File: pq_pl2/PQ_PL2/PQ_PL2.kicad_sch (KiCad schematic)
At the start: 70 parts, among them J1 SLW-110-01-T-S, J2 SLW-110-01-T-S, J3 SLW-110-01-T-S, J4 SLW-110-01-T-S, J5 U.FL-R-SMT, J6 MS-156C3, J7 MS-156C3, J8 MS-156C3, J9 MS-156C3, U1 LEE2-6+, U10 TPS613226ADBVT, U11 TPS613226ADBVT, U12 TCN75AVUA713-VAO, U2 LEE2-6+, U3 LM258WDT, U4 ADE-11X+, U5 LEE2-6+, U6 LT5537EDDB, U8 LT1949ES8#PBF, U9 LT1949ES8#PBF

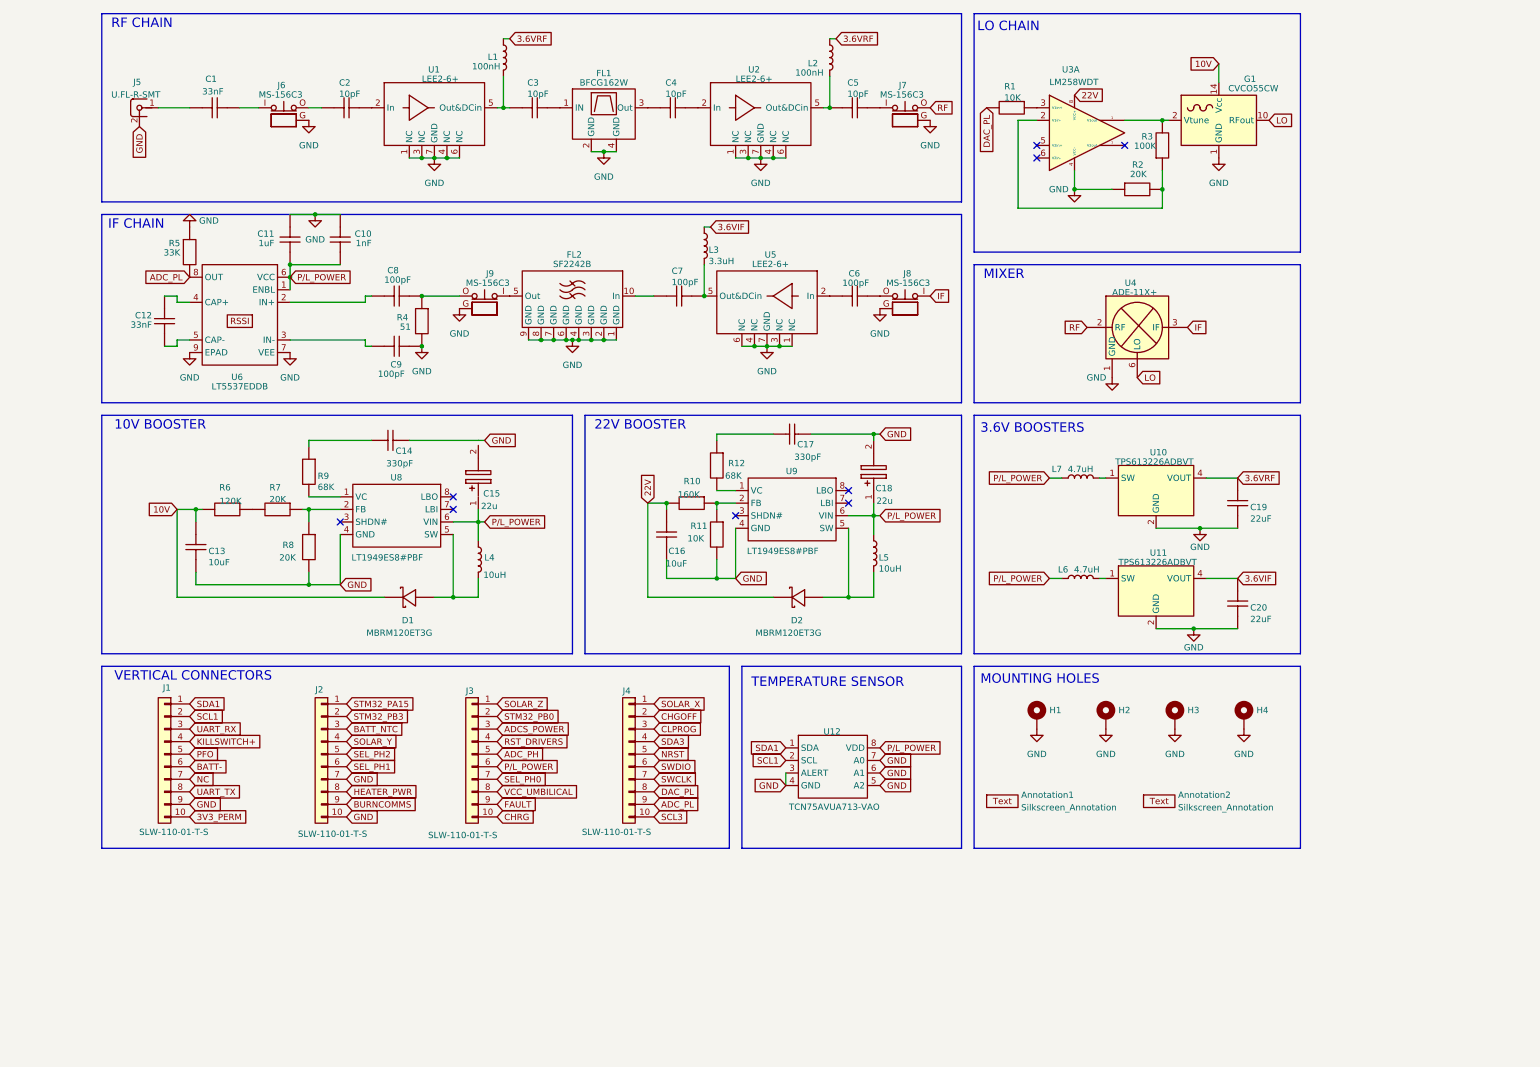
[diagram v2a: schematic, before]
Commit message: P/L2 V03 final schematic. Replaced the Mixer+VCO+Opamp <- OBC DAC configuration with the MAX2121. Switched the IF from 40 MHz (prone to image frequencies due to passive mixers) to 70 MHz with complex mixers with Cheby filter at 75 ohms. Simplified the power supply scheme. Pending PCB & Verification
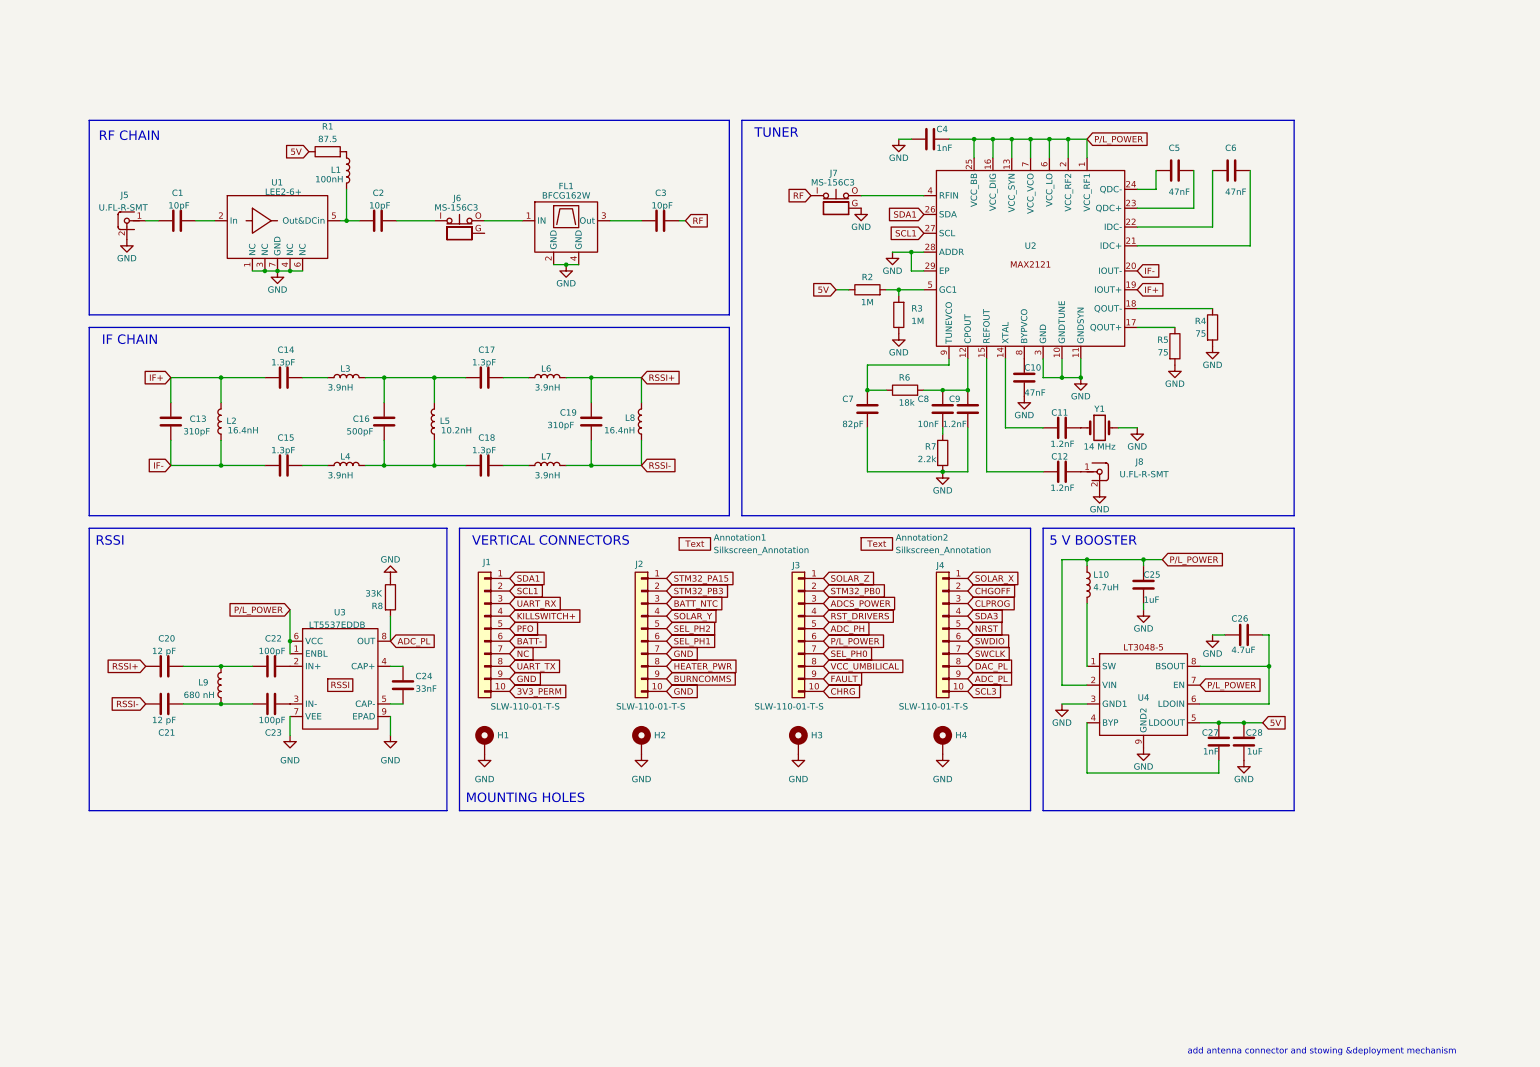
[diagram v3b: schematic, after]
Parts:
- removed C1: 33nF, Capacitor_SMD:C_0603_1608Metric, symbol L2_PCB-altium-import:3_33nF
- removed C10: 1nF, Capacitor_SMD:C_0603_1608Metric, symbol L2_PCB-altium-import:2_1nF
- removed C11: 1uF, Capacitor_SMD:C_0603_1608Metric, symbol L2_PCB-altium-import:2_1uF
- removed C13, C16: 10uF, Capacitor_SMD:C_0603_1608Metric, symbol L2_PCB-altium-import:1_10uF
- removed C14: 330pF, Capacitor_SMD:C_0603_1608Metric, symbol L2_PCB-altium-import:0_330pF
- removed C15, C18: 22u, Capacitor_SMD:C_1206_3216Metric, symbol L2_PCB-altium-import:1_22u
- removed C17: 330pF, Capacitor_SMD:C_0603_1608Metric, symbol L2_PCB-altium-import:2_330pF
- removed C19, C20: 22uF, Capacitor_SMD:C_0603_1608Metric, symbol L2_PCB-altium-import:0_22uF
- removed C5: 10pF, Capacitor_SMD:C_0603_1608Metric, symbol L2_PCB-altium-import:0_10pF
- removed C6, C7: 100pF, Capacitor_SMD:C_0603_1608Metric, symbol L2_PCB-altium-import:0_100pF
- removed D1, D2: MBRM120ET3G, -nsl_passive:MBRM120ET3G, symbol passive-nsl:MBRM120ET3G
- removed FL2: SF2242B, -nsl_rf:SF2242B, symbol rf-nsl:SF2242B
- removed G1: CVCO55CW, RF_Mini-Circuits:Mini-Circuits_CK605_LandPatternPL-012, symbol Oscillator:CVCO55xx
- removed J7, J8, J9: MS-156C3, -nsl_connector:CoaxialSwitch_Hirose_MS-156C3_Horizontal, symbol connector-nsl:MS-156C
- removed R1: 10K, Resistor_SMD:R_0603_1608Metric, symbol L2_PCB-altium-import:2_10K
- removed R10: 160K, Resistor_SMD:R_0603_1608Metric, symbol L2_PCB-altium-import:0_160K
- removed R11: 10K, Resistor_SMD:R_0603_1608Metric, symbol L2_PCB-altium-import:1_10K
- removed R12: 68K, Resistor_SMD:R_0603_1608Metric, symbol L2_PCB-altium-import:3_68K
- removed R2: 20K, Resistor_SMD:R_0603_1608Metric, symbol L2_PCB-altium-import:3_20K
- removed R3: 100K, Resistor_SMD:R_0603_1608Metric, symbol L2_PCB-altium-import:1_100K
- removed R4: 51, Resistor_SMD:R_0603_1608Metric, symbol L2_PCB-altium-import:3_51
- removed R6: 120K, Resistor_SMD:R_0603_1608Metric, symbol L2_PCB-altium-import:0_120K
- removed R7: 20K, Resistor_SMD:R_0603_1608Metric, symbol L2_PCB-altium-import:0_20K
- removed R8: 20K, Resistor_SMD:R_0603_1608Metric, symbol L2_PCB-altium-import:1_20K
- removed R9: 68K, Resistor_SMD:R_0603_1608Metric, symbol L2_PCB-altium-import:1_68K
- removed U10, U11: TPS613226ADBVT, Package_TO_SOT_SMD:SOT-23-5, symbol Regulator_Switching:TPS613226ADBV
- removed U12: TCN75AVUA713-VAO, Package_SO:SOP-8_3.9x4.9mm_P1.27mm, symbol SP_ICs:TCN75AVUA713
- removed U2, U5: LEE2-6+, Package_SON:WSON-6-1EP_2x2mm_P0.65mm_EP1x1.6mm, symbol rf-nsl:LEE2-6+
- removed U3: LM258WDT, Package_SO:SO-8_3.9x4.9mm_P1.27mm, symbol power-nsl:LM258
- removed U4: ADE-11X+, -nsl_rf:SOTFL254P691X284-6N, symbol rf-nsl:ADE-11X
- removed U8, U9: LT1949ES8#PBF, Package_SO:SO-8_3.9x4.9mm_P1.27mm, symbol power-nsl:LT1949
- added C10, C5, C6: 47nF, Capacitor_SMD:C_0603_1608Metric, symbol Device:C
- added C11, C12, C9: 1.2nF, Capacitor_SMD:C_0603_1608Metric, symbol Device:C
- added C13, C19: 310pF, Capacitor_SMD:C_0603_1608Metric, symbol Device:C
- added C14, C15, C17, C18: 1.3pF, Capacitor_SMD:C_0603_1608Metric, symbol Device:C
- added C16: 500pF, Capacitor_SMD:C_0603_1608Metric, symbol Device:C
- added C20, C21: 12 pF, Capacitor_SMD:C_0603_1608Metric, symbol Device:C
- added C25, C28: 1uF, Capacitor_SMD:C_0603_1608Metric, symbol Device:C
- added C26: 4.7uF, Capacitor_SMD:C_0603_1608Metric, symbol Device:C
- added C27, C4: 1nF, Capacitor_SMD:C_0603_1608Metric, symbol Device:C
- added C7: 82pF, Capacitor_SMD:C_0603_1608Metric, symbol Device:C
- added C8: 10nF, Capacitor_SMD:C_0603_1608Metric, symbol Device:C
- added J7: MS-156C3, -nsl_connector:CoaxialSwitch_Hirose_MS-156C3_Horizontal, symbol -nsl_connector:MS-156C
- added J8: U.FL-R-SMT, -nsl_connector:C.FL-R-SMT-1(90), symbol -nsl_connector:connector-coax
- added L10: 4.7uH, Inductor_SMD:L_0603_1608Metric, symbol Device:L
- added L8: 16.4nH, Inductor_SMD:L_0603_1608Metric, symbol Device:L
- added L9: 680 nH, Inductor_SMD:L_0603_1608Metric, symbol Device:L
- added R1: 87.5, Resistor_SMD:R_0612_1632Metric, symbol Device:R
- added R2, R3: 1M, Resistor_SMD:R_0612_1632Metric, symbol Device:R
- added R4, R5: 75, Resistor_SMD:R_0612_1632Metric, symbol Device:R
- added R6: 18k, Resistor_SMD:R_0612_1632Metric, symbol Device:R
- added R7: 2.2k, Resistor_SMD:R_0612_1632Metric, symbol Device:R
- added U2: ~, -nsl_rf:QFN50P500X500X80-29N, symbol -nsl_rf:MAX2121
- added U4: ~, -nsl_power:SON45P200X200X80-9N, symbol -nsl_power:LT3048
- added Y1: 14 MHz, symbol Device:Crystal
- Annotation1, Annotation2: symbol symbols-nsl:Silkscreen_Annotation -> -nsl_symbols:Silkscreen_Annotation
- C1: renamed from C2; symbol L2_PCB-altium-import:0_10pF -> Device:C
- C2: renamed from C3; symbol L2_PCB-altium-import:0_10pF -> Device:C
- C22: renamed from C8; symbol L2_PCB-altium-import:0_100pF -> Device:C
- C23: renamed from C9; symbol L2_PCB-altium-import:0_100pF -> Device:C
- C24: renamed from C12; symbol L2_PCB-altium-import:2_33nF -> Device:C
- C3: renamed from C4; symbol L2_PCB-altium-import:0_10pF -> Device:C
- FL1: symbol rf-nsl:BFCG162W -> -nsl_rf:BFCG162W
- J1, J2, J3, J4: footprint -nsl_connector:BBL-110-Y-X -> -nsl_connector:SLW-110-01; symbol connector-nsl:SLW-110-01 -> -nsl_connector:SLW-110-01
- J5: symbol connector-nsl:connector-coax -> -nsl_connector:connector-coax
- J6: symbol connector-nsl:MS-156C -> -nsl_connector:MS-156C
- L2: value 100nH -> 16.4nH
- L3: value 3.3uH -> 3.9nH; BOM_MANUFACTURER Yanchuang -> Sunlord; BOM_MANUFACTURER PART SCMI160808U1R0KT -> SDFL1005LR10KTF; BOM_SUPPLIER PART C479880 -> C370259; SPICESYMBOLNAME SCMI160808U1R0KT -> SDFL1005LR10KTF
- L4: value 10uH -> 3.9nH; BOM_MANUFACTURER Murata Electronics -> Sunlord; BOM_MANUFACTURER PART LQM18PN2R2NC0L -> SDFL1005LR10KTF; BOM_SUPPLIER PART C162580 -> C370259; SPICESYMBOLNAME LQM18PN2R2NC0L -> SDFL1005LR10KTF
- L5: value 10uH -> 10.2nH; BOM_MANUFACTURER Murata Electronics -> Sunlord; BOM_MANUFACTURER PART LQM18PN2R2NC0L -> SDFL1005LR10KTF; BOM_SUPPLIER PART C162580 -> C370259; SPICESYMBOLNAME LQM18PN2R2NC0L -> SDFL1005LR10KTF
- L6, L7: value 4.7uH -> 3.9nH; BOM_MANUFACTURER Taiyo Yuden -> Sunlord; BOM_MANUFACTURER PART CBC2012T4R7M -> SDFL1005LR10KTF; BOM_SUPPLIER PART C92978 -> C370259; SPICESYMBOLNAME CBC2012T4R7M -> SDFL1005LR10KTF
- R8: renamed from R5; symbol L2_PCB-altium-import:2_33K -> Device:R
- U1: symbol rf-nsl:LEE2-6+ -> -nsl_rf:LEE2-6+
- U3: renamed from U6; symbol rf-nsl:LT5537 -> -nsl_rf:LT5537
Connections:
- net GND: now also C10.2, C25.2, C26.2, C28.1, C4.2, C7.2, C9.2, J7.G, J8.2, R3.1, R4.2, R5.2, R7.2, U2.10 (GNDTUNE), U2.11 (GNDSYN), U2.28 (ADDR), U2.29 (EP), U2.3 (GND), U4.3 (GND1), U4.9 (GND2), Y1.2; no longer C23.2, J6.G
- net P/L_POWER: now also C25.1, C4.1, L10.1, U2.1 (VCC_RF1), U2.13 (VCC_SYN), U2.16 (VCC_DIG), U2.2 (VCC_RF2), U2.25 (VCC_BB), U2.6 (VCC_LO), U2.7 (VCC_VCO), U4.2 (VIN), U4.7 (EN); no longer L4.1, L5.1, L6.1, L7.1
- net RF: now also C3.2, J7.I
- net SCL1: now also U2.27 (SCL)
- net SDA1: now also U2.26 (SDA)
- net at L5.2: now also L4.1, C16.1, C18.2
- net at L6.2: now also C17.1
- net at C22.2: now also C20.1, L9.2
- net IF-: now reaches L2.2
- net IF-: now also C13.1, C15.2, U2.20 (IOUT-)
- net at U3.4 (CAP+): now also C24.2; no longer C24.1
- net at U3.5 (CAP-): now also C24.1; no longer C24.2
- net at L7.2: now also C18.1
- net at L4.2: now also C15.1
- net at J6.I: now also C2.2
- net at J5.1: now also C1.1
- net at J6.O: now also FL1.1 (IN); no longer C1.1
- net at L3.2: now also C14.1
- net 3.6VIF: no longer names the net of L3.1
- net 3.6VIF: now also L5.1, C16.2, C17.2
- net 3.6VRF: no longer names the net of L1.1
- net 3.6VRF: now also R1.2; no longer L2.1
- new net: C11.1, U2.14 (XTAL)
- new net: C11.2, Y1.1
- new net: R4.1, U2.18 (QOUT-)
- new net: C21.1, C23.2, L9.1
- new net: C27.1, U4.4 (BYP)
- new net: C12.1, U2.15 (REFOUT)
- new net: C12.2, J8.1
- new net: C8.1, C9.1, R6.2, U2.12 (CPOUT)
- new net: C8.2, R7.1
- new net: C7.1, R6.1, U2.9 (TUNEVCO)
- new net: L10.2, U4.1 (SW)
- new net: C26.1, U4.6 (LDOIN), U4.8 (BSOUT)
- new net: C10.1, U2.8 (BYPVCO)
- new net: R2.2, R3.2, U2.5 (GC1)
- new net: C5.1, U2.23 (QDC+)
- new net: C5.2, U2.24 (QDC-)
- new net: C6.1, U2.21 (IDC+)
- new net: C6.2, U2.22 (IDC-)
- new net: R5.1, U2.17 (QOUT+)
- new net: J7.O, U2.4 (RFIN)
- new net 5V: C27.2, C28.2, R1.1, R2.1, U4.5 (LDOOUT)
- new net IF+: C13.2, C14.2, L2.1, U2.19 (IOUT+)
- new net RSSI+: C19.2, C20.2, L6.1, L8.1
- new net RSSI-: C19.1, C21.2, L7.1, L8.2
- no-connect marks 9 -> 0
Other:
- note added: "5 V BOOSTER"
- note added: "RSSI"
- note added: "TUNER"
- note added: "add antenna connector and stowing &deployment mechanism"
- note removed: "10V BOOSTER"
- note removed: "22V BOOSTER"
- note removed: "3.6V BOOSTERS"
- note removed: "LO CHAIN"
- note removed: "MIXER"
- note removed: "TEMPERATURE SENSOR"
- moved on the sheet: Annotation1, Annotation2, FL1, H1, H2, H3, H4, J1, J2, J3, J4, J5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

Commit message: P/L2 schematic revision and preliminary layout formulation: tranmission lines and block biasing
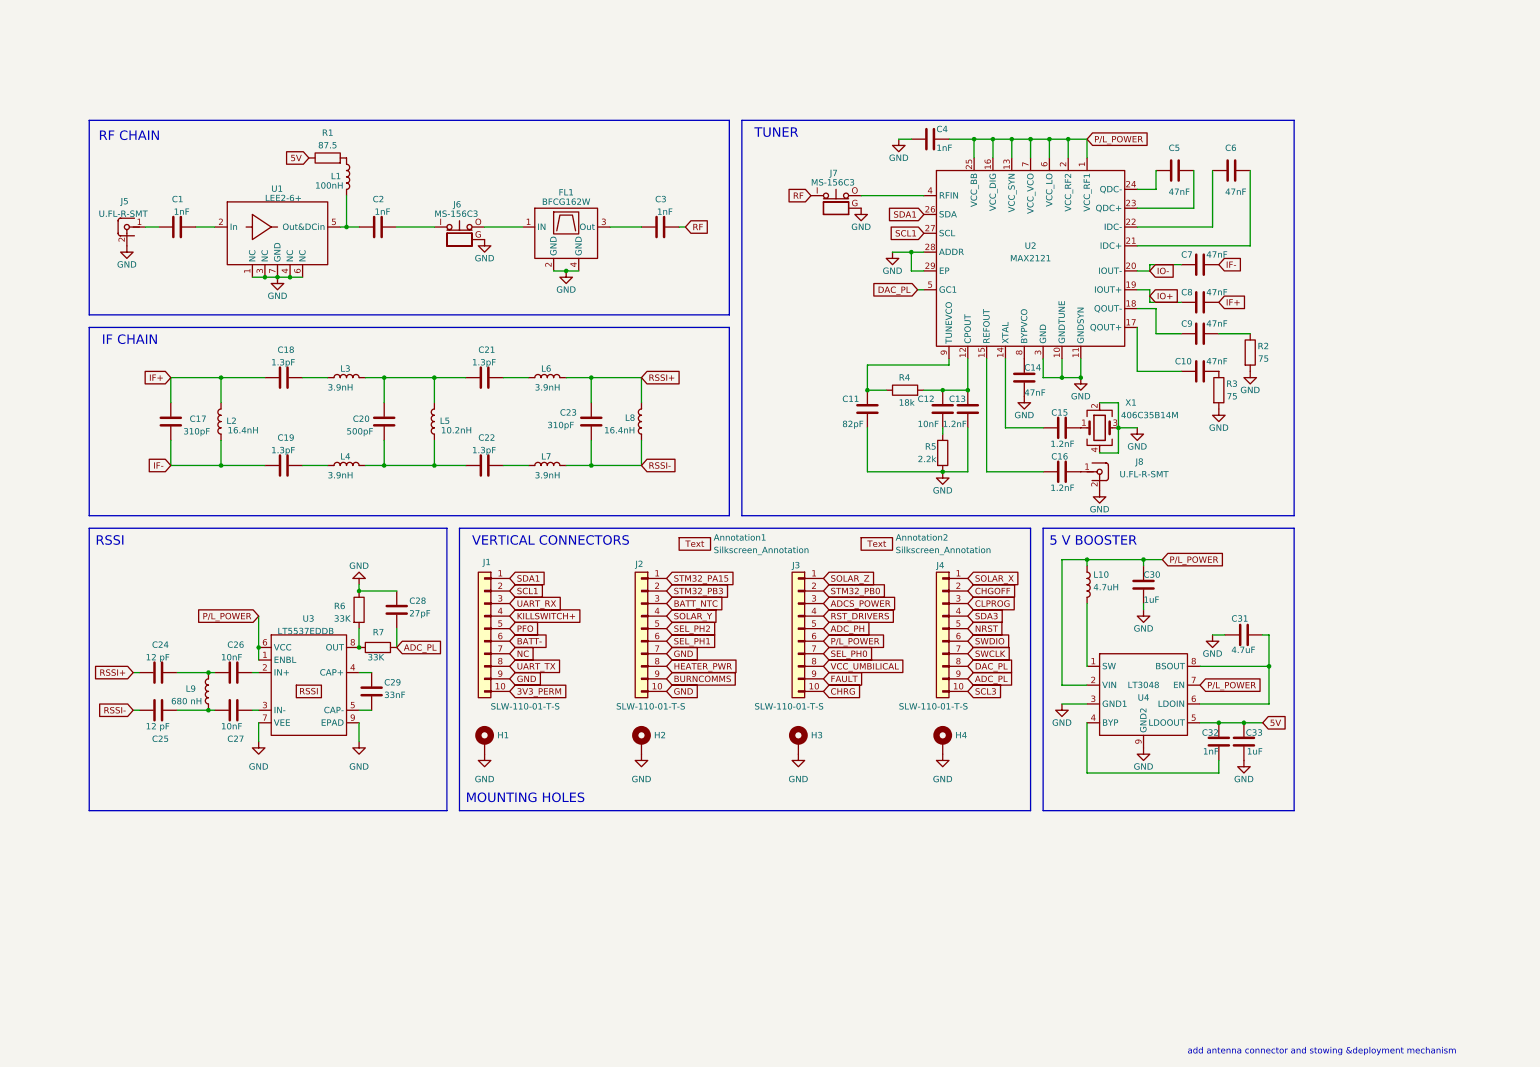
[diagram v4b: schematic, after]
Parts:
- removed R4, R5: 75, Resistor_SMD:R_0612_1632Metric, symbol Device:R
- removed Y1: 14 MHz, symbol Device:Crystal
- added C10, C7, C8, C9: 47nF, Capacitor_SMD:C_0603_1608Metric, symbol Device:C
- added C28: 27pF, Capacitor_SMD:C_0603_1608Metric, symbol Device:C
- added R7: 33K, Resistor_SMD:R_0603_1608Metric, symbol Device:R
- added X1: 406C35B14M, -nsl_miscellaneous:406C35B14M, symbol -nsl_miscellaneous:406C35B14M
- C1, C2, C3: value 10pF -> 1nF
- C26: renamed from C22; value 100pF -> 10nF
- C27: renamed from C23; value 100pF -> 10nF
- R1: footprint Resistor_SMD:R_0612_1632Metric -> Resistor_SMD:R_0603_1608Metric
- R2, R3: value 1M -> 75; footprint Resistor_SMD:R_0612_1632Metric -> Resistor_SMD:R_0603_1608Metric
- R4: renamed from R6; footprint Resistor_SMD:R_0612_1632Metric -> Resistor_SMD:R_0603_1608Metric
- R5: renamed from R7; footprint Resistor_SMD:R_0612_1632Metric -> Resistor_SMD:R_0603_1608Metric
- U2: value ~ -> MAX2121
- U4: value ~ -> LT3048
- renumbered C7 to C11, C8 to C12, C9 to C13, C10 to C14, C11 to C15, C12 to C16, C13 to C17, C14 to C18, C15 to C19, C16 to C20, C17 to C21, C18 to C22, C19 to C23, C20 to C24, C21 to C25, C24 to C29, C25 to C30, C26 to C31, C27 to C32, C28 to C33, R8 to R6
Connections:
- net 5V: no longer R2.1
- net ADC_PL: now also C28.1, R7.2; no longer R6.2, U3.8 (OUT)
- net DAC_PL: now also U2.5 (GC1)
- net GND: now also J6.G, R2.2, R3.2, C28.2, X1.2, X1.3, X1.4; no longer R3.1
- net IF+: now also C8.1; no longer U2.19 (IOUT+)
- net IF-: now also C7.1; no longer U2.20 (IOUT-)
- net at C15.2: now also X1.1
- net at U2.18 (QOUT-): now also C9.2
- net at U2.17 (QOUT+): now also C10.2
- new net: C10.1, R3.1
- new net: R6.2, R7.1, U3.8 (OUT)
- new net: C9.1, R2.1
- new net IO+: C8.2, U2.19 (IOUT+)
- new net IO-: C7.2, U2.20 (IOUT-)
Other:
- moved on the sheet: C1, C2, C24, C25, C26, C27, C29, C3, FL1, J5, J6, L1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
